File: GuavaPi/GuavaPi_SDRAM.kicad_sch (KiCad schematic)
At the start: 5 parts, among them IC1 D2516ECMDXGJD-U, IC2 D2516ECMDXGJD-U

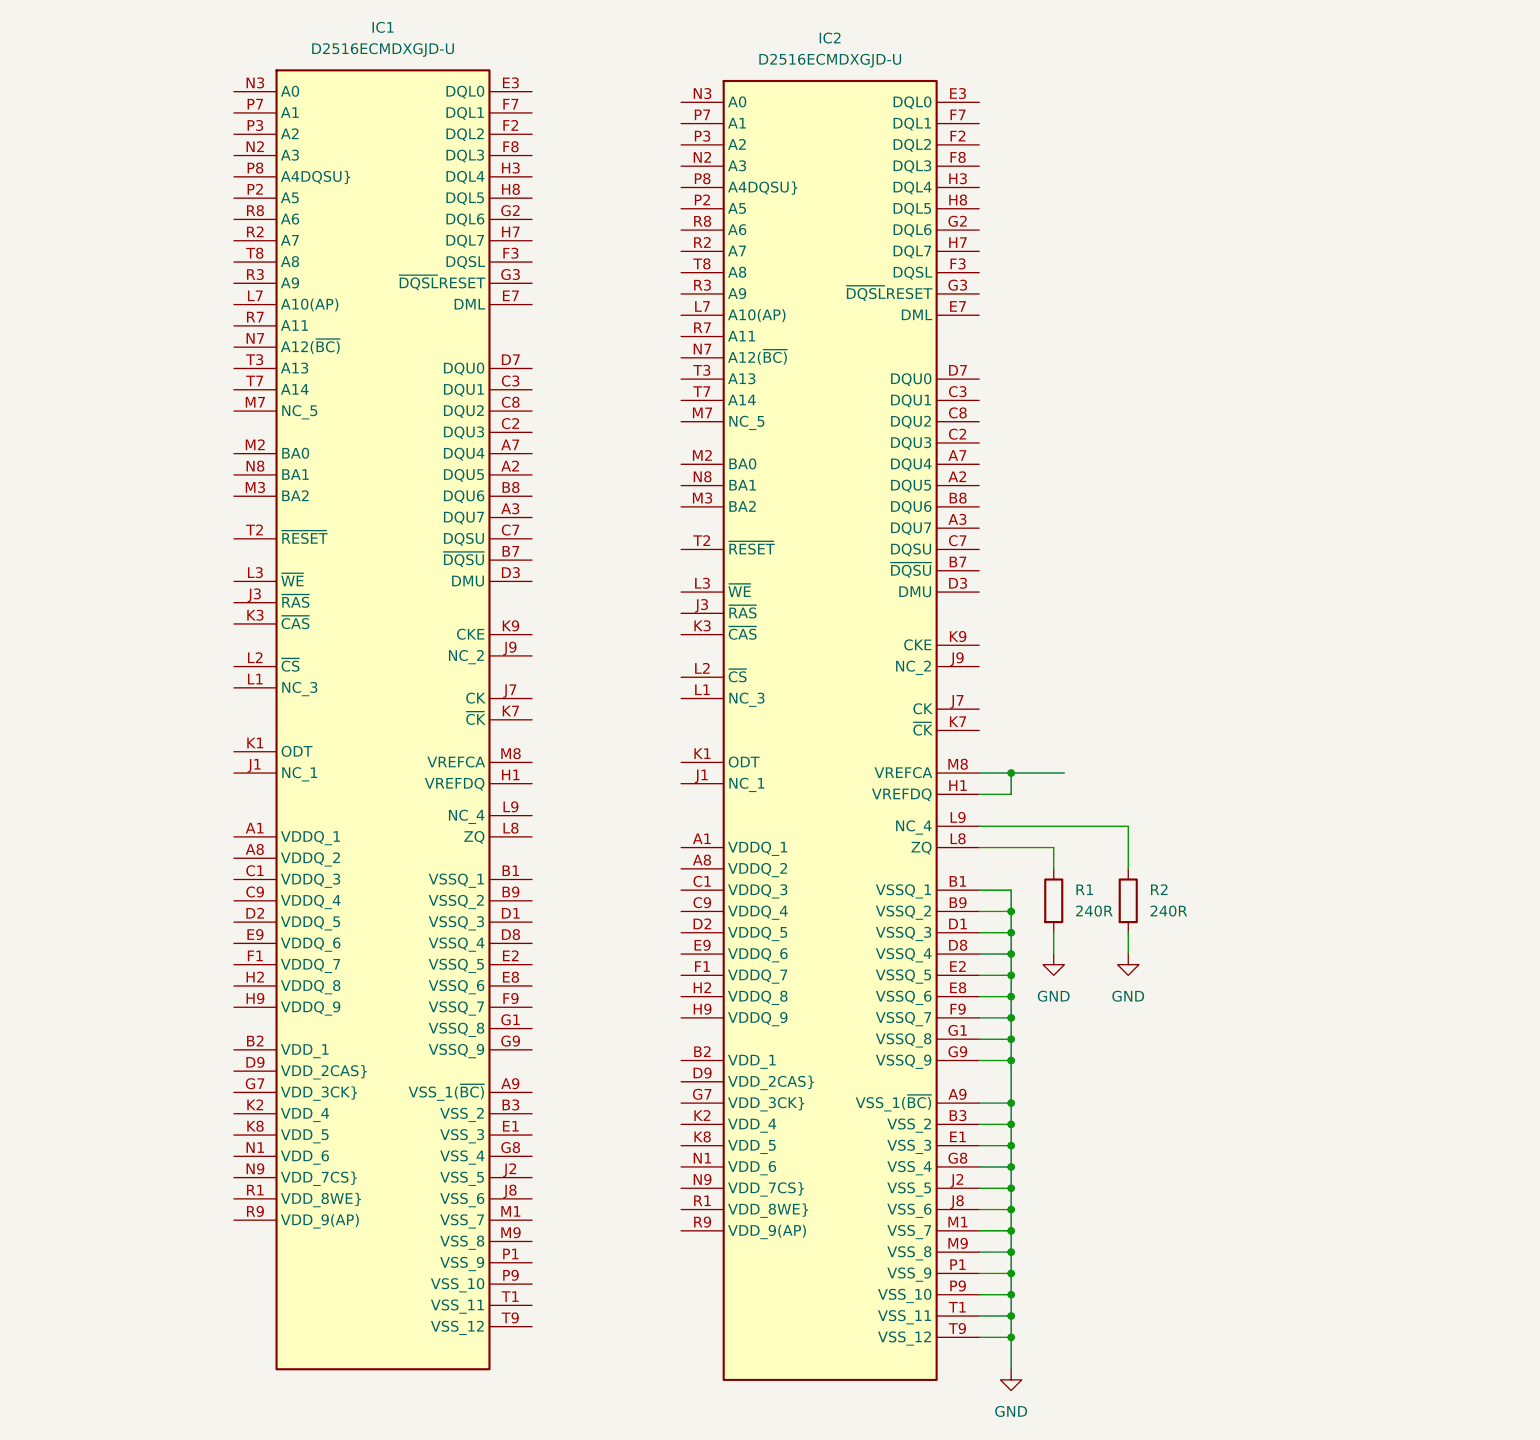
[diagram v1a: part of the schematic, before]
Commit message: DDR3 Module Power & Pinout
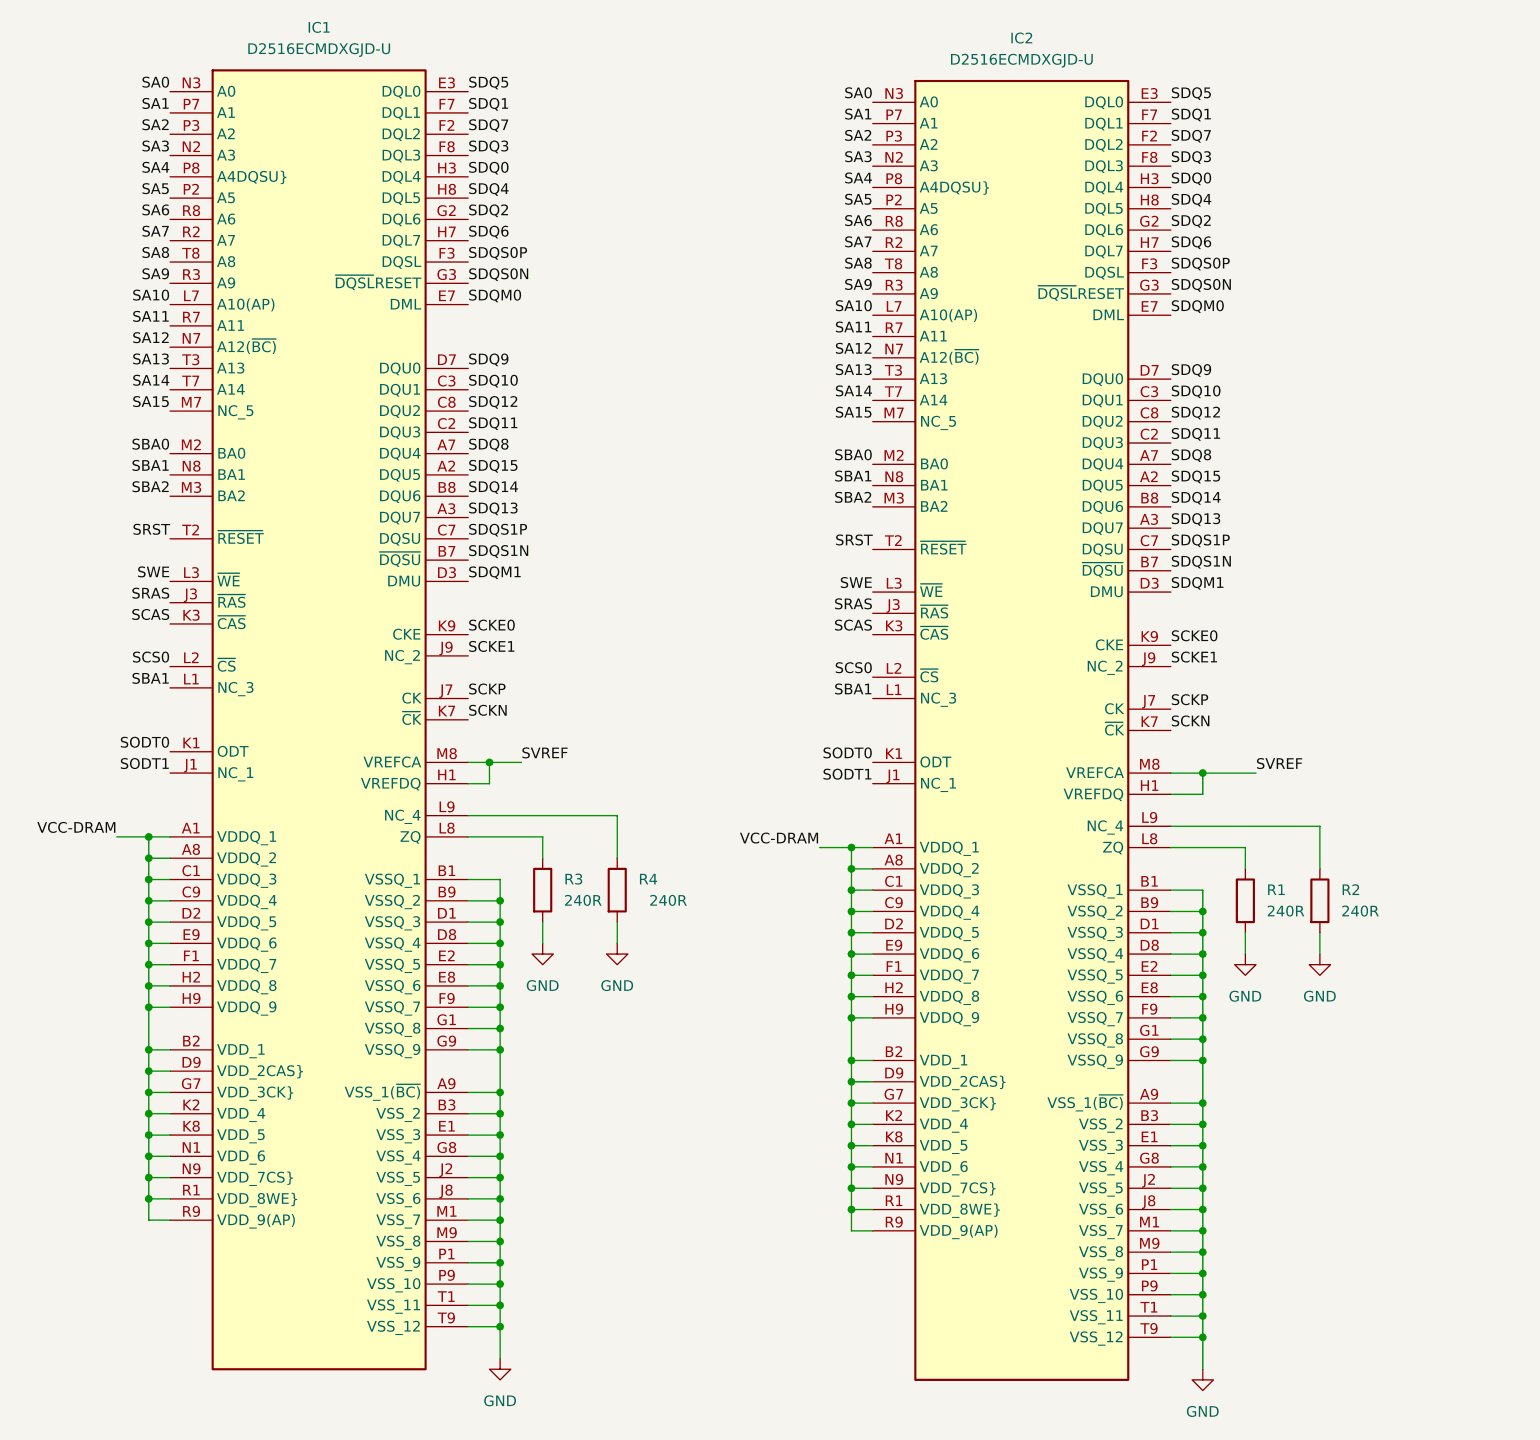
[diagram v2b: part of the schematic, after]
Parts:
- added R3, R4: 240R, symbol Device:R
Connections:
- net GND: now also IC1.A9 (VSS_1(~{BC)}), IC1.B1 (VSSQ_1), IC1.B3 (VSS_2), IC1.B9 (VSSQ_2), IC1.D1 (VSSQ_3), IC1.D8 (VSSQ_4), IC1.E1 (VSS_3), IC1.E2 (VSSQ_5), IC1.E8 (VSSQ_6), IC1.F9 (VSSQ_7), IC1.G1 (VSSQ_8), IC1.G8 (VSS_4), IC1.G9 (VSSQ_9), IC1.J2 (VSS_5), IC1.J8 (VSS_6), IC1.M1 (VSS_7), IC1.M9 (VSS_8), IC1.P1 (VSS_9), IC1.P9 (VSS_10), IC1.T1 (VSS_11), IC1.T9 (VSS_12), R3.2, R4.2
- net VCC-DRAM: now reaches IC1.A1 (VDDQ_1)
- net VCC-DRAM: now also IC1.A8 (VDDQ_2), IC1.B2 (VDD_1), IC1.C1 (VDDQ_3), IC1.C9 (VDDQ_4), IC1.D2 (VDDQ_5), IC1.D9 (VDD_2CAS}), IC1.E9 (VDDQ_6), IC1.F1 (VDDQ_7), IC1.G7 (VDD_3CK}), IC1.H2 (VDDQ_8), IC1.H9 (VDDQ_9), IC1.K2 (VDD_4), IC1.K8 (VDD_5), IC1.N1 (VDD_6), IC1.N9 (VDD_7CS}), IC1.R1 (VDD_8WE}), IC1.R9 (VDD_9(AP)), IC2.A1 (VDDQ_1), IC2.A8 (VDDQ_2), IC2.B2 (VDD_1), IC2.C1 (VDDQ_3), IC2.C9 (VDDQ_4), IC2.D2 (VDDQ_5), IC2.D9 (VDD_2CAS}), IC2.E9 (VDDQ_6), IC2.F1 (VDDQ_7), IC2.G7 (VDD_3CK}), IC2.H2 (VDDQ_8), IC2.H9 (VDDQ_9), IC2.K2 (VDD_4), IC2.K8 (VDD_5), IC2.N1 (VDD_6), IC2.N9 (VDD_7CS}), IC2.R1 (VDD_8WE}), IC2.R9 (VDD_9(AP))
- net SDQ15: now reaches IC1.A2 (DQU5)
- net SDQ15: now also IC2.A2 (DQU5)
- net SDQ13: now reaches IC1.A3 (DQU7)
- net SDQ13: now also IC2.A3 (DQU7)
- net SDQ8: now reaches IC1.A7 (DQU4)
- net SDQ8: now also IC2.A7 (DQU4)
- net SDQS1N: now reaches IC1.B7 (~{DQSU})
- net SDQS1N: now also IC2.B7 (~{DQSU})
- net SDQ14: now reaches IC1.B8 (DQU6)
- net SDQ14: now also IC2.B8 (DQU6)
- net SDQ11: now reaches IC1.C2 (DQU3)
- net SDQ11: now also IC2.C2 (DQU3)
- net SDQ10: now reaches IC1.C3 (DQU1)
- net SDQ10: now also IC2.C3 (DQU1)
- net SDQS1P: now reaches IC1.C7 (DQSU)
- net SDQS1P: now also IC2.C7 (DQSU)
- net SDQ12: now reaches IC1.C8 (DQU2)
- net SDQ12: now also IC2.C8 (DQU2)
- net SDQM1: now reaches IC1.D3 (DMU)
- net SDQM1: now also IC2.D3 (DMU)
- net SDQ9: now reaches IC1.D7 (DQU0)
- net SDQ9: now also IC2.D7 (DQU0)
- net SDQ5: now reaches IC1.E3 (DQL0)
- net SDQ5: now also IC2.E3 (DQL0)
- net SDQM0: now reaches IC1.E7 (DML)
- net SDQM0: now also IC2.E7 (DML)
- net SDQ7: now reaches IC1.F2 (DQL2)
- net SDQ7: now also IC2.F2 (DQL2)
- net SDQS0P: now reaches IC1.F3 (DQSL)
- net SDQS0P: now also IC2.F3 (DQSL)
- net SDQ1: now reaches IC1.F7 (DQL1)
- net SDQ1: now also IC2.F7 (DQL1)
- net SDQ3: now reaches IC1.F8 (DQL3)
- net SDQ3: now also IC2.F8 (DQL3)
- net SDQ2: now reaches IC1.G2 (DQL6)
- net SDQ2: now also IC2.G2 (DQL6)
- net SDQS0N: now reaches IC1.G3 (~{DQSL}RESET)
- net SDQS0N: now also IC2.G3 (~{DQSL}RESET)
- net SVREF: now reaches IC1.H1 (VREFDQ)
- net SVREF: now also IC1.M8 (VREFCA), IC2.H1 (VREFDQ), IC2.M8 (VREFCA)
- net SDQ0: now reaches IC1.H3 (DQL4)
- net SDQ0: now also IC2.H3 (DQL4)
- net SDQ6: now reaches IC1.H7 (DQL7)
- net SDQ6: now also IC2.H7 (DQL7)
- net SDQ4: now reaches IC1.H8 (DQL5)
- net SDQ4: now also IC2.H8 (DQL5)
- net SODT1: now reaches IC1.J1 (NC_1)
- net SODT1: now also IC2.J1 (NC_1)
- net SRAS: now reaches IC1.J3 (~{RAS})
- net SRAS: now also IC2.J3 (~{RAS})
- net SCKP: now reaches IC1.J7 (CK)
- net SCKP: now also IC2.J7 (CK)
- net SCKE1: now reaches IC1.J9 (NC_2)
- net SCKE1: now also IC2.J9 (NC_2)
- net SODT0: now reaches IC1.K1 (ODT)
- net SODT0: now also IC2.K1 (ODT)
- net SCAS: now reaches IC1.K3 (~{CAS})
- net SCAS: now also IC2.K3 (~{CAS})
- net SCKN: now reaches IC1.K7 (~{CK})
- net SCKN: now also IC2.K7 (~{CK})
- net SCKE0: now reaches IC1.K9 (CKE)
- net SCKE0: now also IC2.K9 (CKE)
- net SBA1: now reaches IC1.L1 (NC_3)
- net SBA1: now also IC1.N8 (BA1), IC2.L1 (NC_3), IC2.N8 (BA1)
- net SCS0: now reaches IC1.L2 (~{CS})
- net SCS0: now also IC2.L2 (~{CS})
- net SWE: now reaches IC1.L3 (~{WE})
- net SWE: now also IC2.L3 (~{WE})
- net SA10: now reaches IC1.L7 (A10(AP))
- net SA10: now also IC2.L7 (A10(AP))
- net at IC1.L8 (ZQ): now also R3.1
- net at IC1.L9 (NC_4): now also R4.1
- net SBA0: now reaches IC1.M2 (BA0)
- net SBA0: now also IC2.M2 (BA0)
- net SBA2: now reaches IC1.M3 (BA2)
- net SBA2: now also IC2.M3 (BA2)
- net SA15: now reaches IC1.M7 (NC_5)
- net SA15: now also IC2.M7 (NC_5)
- net SA3: now reaches IC1.N2 (A3)
- net SA3: now also IC2.N2 (A3)
- net SA0: now reaches IC1.N3 (A0)
- net SA0: now also IC2.N3 (A0)
- net SA12: now reaches IC1.N7 (A12(~{BC)})
- net SA12: now also IC2.N7 (A12(~{BC)})
- net SA5: now reaches IC1.P2 (A5)
- net SA5: now also IC2.P2 (A5)
- net SA2: now reaches IC1.P3 (A2)
- net SA2: now also IC2.P3 (A2)
- net SA1: now reaches IC1.P7 (A1)
- net SA1: now also IC2.P7 (A1)
- net SA4: now reaches IC1.P8 (A4DQSU})
- net SA4: now also IC2.P8 (A4DQSU})
- net SA7: now reaches IC1.R2 (A7)
- net SA7: now also IC2.R2 (A7)
- net SA9: now reaches IC1.R3 (A9)
- net SA9: now also IC2.R3 (A9)
- net SA11: now reaches IC1.R7 (A11)
- net SA11: now also IC2.R7 (A11)
- net SA6: now reaches IC1.R8 (A6)
- net SA6: now also IC2.R8 (A6)
- net SRST: now reaches IC1.T2 (~{RESET})
- net SRST: now also IC2.T2 (~{RESET})
- net SA13: now reaches IC1.T3 (A13)
- net SA13: now also IC2.T3 (A13)
- net SA14: now reaches IC1.T7 (A14)
- net SA14: now also IC2.T7 (A14)
- net SA8: now reaches IC1.T8 (A8)
- net SA8: now also IC2.T8 (A8)
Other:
- moved on the sheet: IC1, IC2, R1, R2
